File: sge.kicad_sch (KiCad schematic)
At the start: 27 parts, among them IC6 315-5660

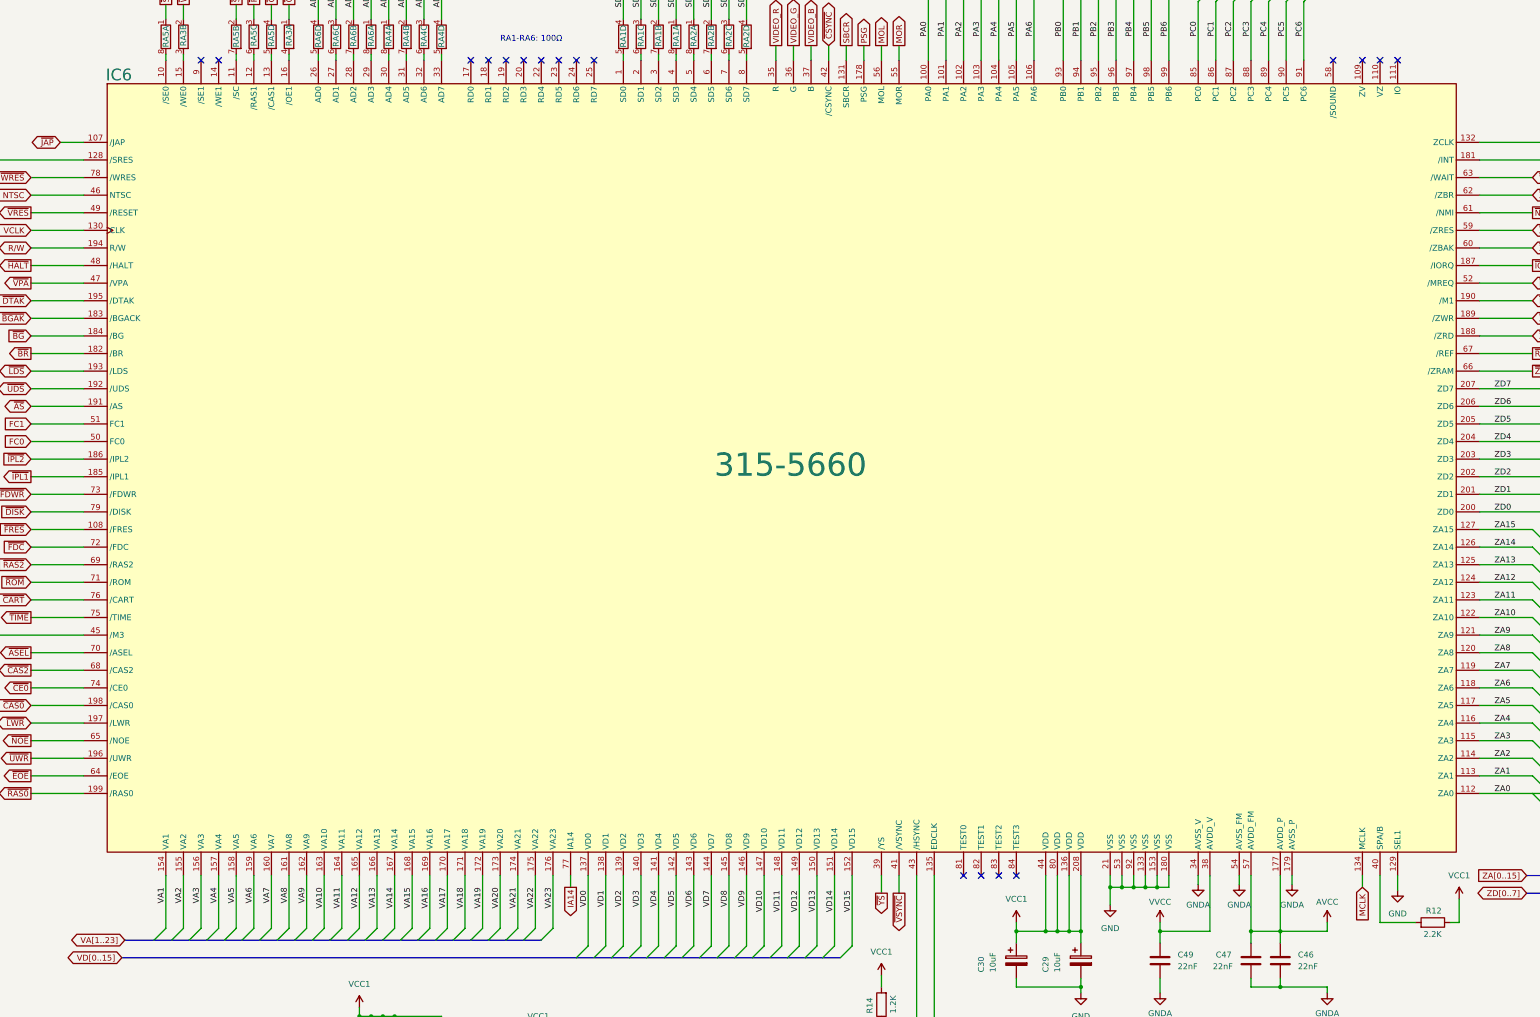
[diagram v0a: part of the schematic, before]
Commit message: update readme, update kicad version, add connection between 81 and GND
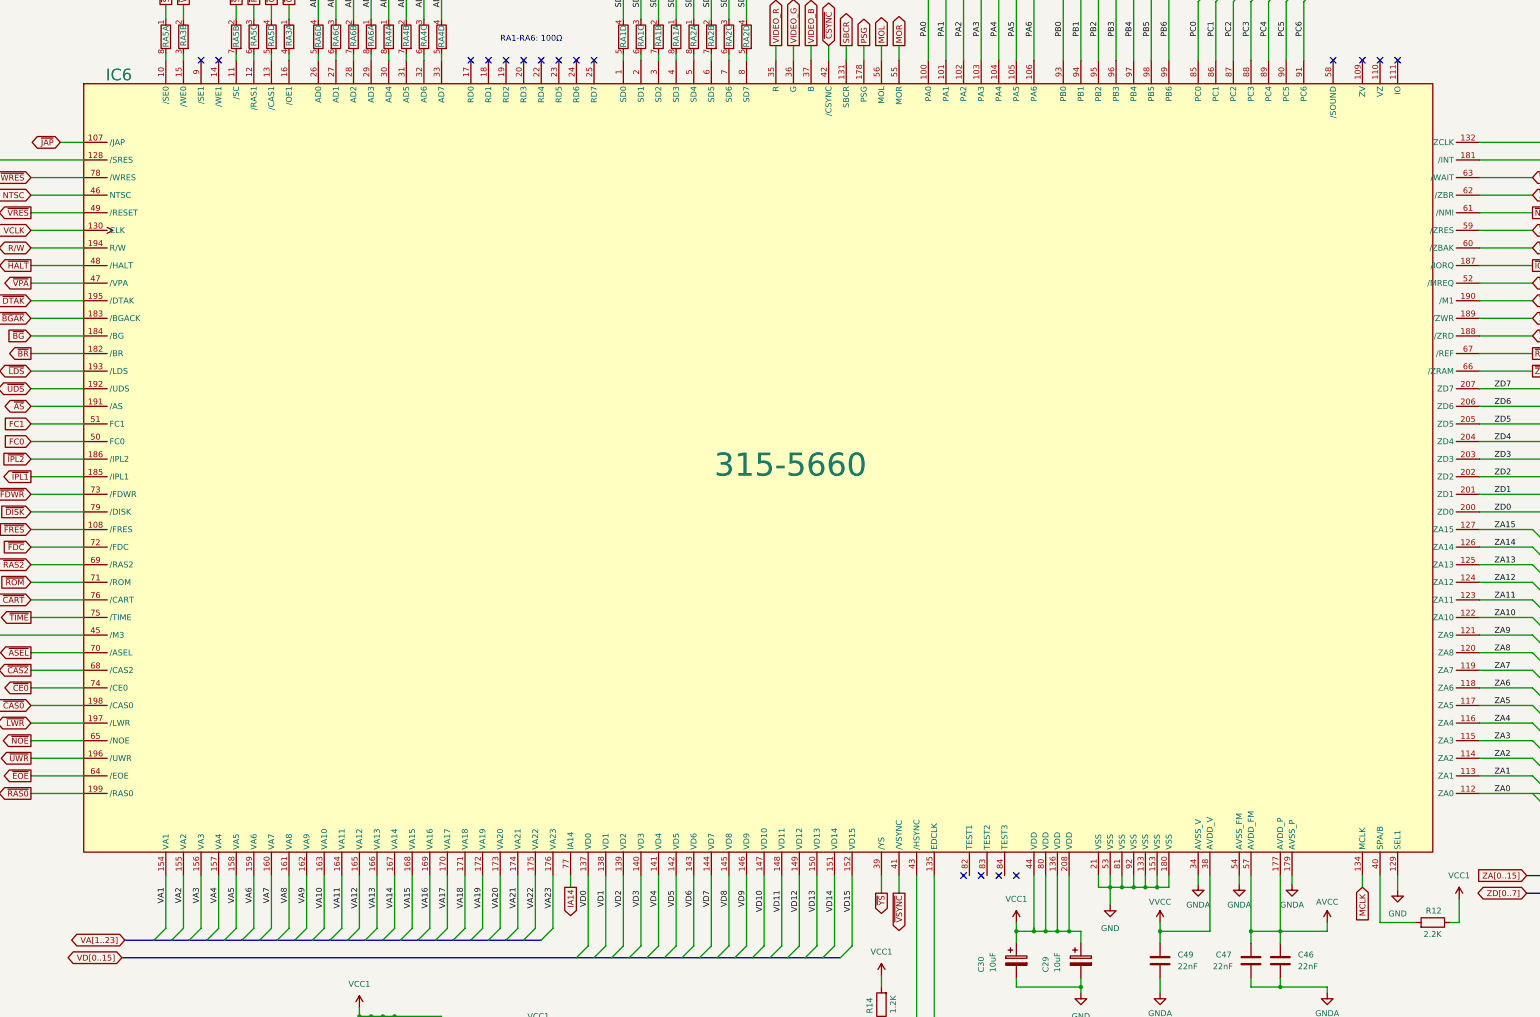
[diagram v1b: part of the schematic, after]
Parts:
- IC6: footprint Neptune:QFP-208_28x28_Pitch0.5mm -> Package_QFP:LQFP-208_28x28mm_P0.5mm
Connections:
- net GND: now also IC6.81 (VSS)
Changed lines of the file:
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@@
 (kicad_sch
-	(version 20231120)
+	(version 20250114)
 	(generator "eeschema")
-	(generator_version "8.0")
+	(generator_version "9.0")
 	(paper "A3")
 	(title_block
@@
 		(comment 1 "Neptune")
 	)
+	(text "Using 32X's RESET means we\ndon't need the whole /MRES\nto /SRES circuit from the MD."
+		(exclude_from_sim no)
+		(at 15.875 61.595 0)
+		(effects
+			(font
+				(size 1.27 1.27)
+			)
+			(justify left bottom)
+		)
+	)
+	(text "RA1-RA6: 100Ω"
+		(exclude_from_sim no)
+		(at 152.4 39.37 0)
+		(effects
+			(font
+				(size 1.27 1.27)
+			)
+			(justify left bottom)
+		)
+	)
 	(junction
 		(at 292.1 222.25)
@@
 	)
 	(junction
+		(at 267.965 231.775)
+		(diameter 0)
+		(color 0 0 0 0)
+	)
+	(junction
 		(at 127 250.19)
 		(diameter 0)
@@
 	)
 	(junction
-		(at 278.13 231.775)
-		(diameter 0)
-		(color 0 0 0 0)
-	)
-	(junction
 		(at 175.26 257.81)
 		(diameter 0)
@@
 	(wire
 		(pts
-			(xy 264.16 231.775) (xy 270.51 231.775)
+			(xy 264.16 231.775) (xy 267.965 231.775)
 		)
 		(stroke
@@
 	(wire
 		(pts
+			(xy 267.965 231.14) (xy 267.965 231.775)
+		)
+		(stroke
+			(width 0)
+			(type default)
+		)
+	)
+	(wire
+		(pts
 			(xy 303.53 219.71) (xy 303.53 221.615)
 		)
@@
 	(wire
 		(pts
-			(xy 87.63 219.71) (xy 87.63 231.14)
+			(xy 267.965 231.775) (xy 270.51 231.775)
 		)
 		(stroke
@@
 	(wire
 		(pts
-			(xy 50.8 133.35) (xy 62.23 133.35)
+			(xy 87.63 219.71) (xy 87.63 231.14)
 		)
 		(stroke
@@
 	(wire
 		(pts
-			(xy 201.93 219.71) (xy 201.93 234.95)
+			(xy 50.8 133.35) (xy 62.23 133.35)
 		)
 		(stroke
@@
 	(wire
 		(pts
-			(xy 50.8 99.06) (xy 62.23 99.06)
+			(xy 201.93 219.71) (xy 201.93 234.95)
 		)
 		(stroke
@@
 		)
 	)
-	(bus
+	(wire
 		(pts
-			(xy 378.46 158.75) (xy 378.46 162.56)
+			(xy 50.8 99.06) (xy 62.23 99.06)
 		)
 		(stroke
@@
 		)
 	)
-	(wire
+	(bus
 		(pts
-			(xy 190.5 41.91) (xy 190.5 43.18)
+			(xy 378.46 158.75) (xy 378.46 162.56)
 		)
 		(stroke
@@
 	(wire
 		(pts
-			(xy 278.13 219.71) (xy 278.13 231.775)
+			(xy 190.5 41.91) (xy 190.5 43.18)
 		)
 		(stroke
@@
 	(wire
 		(pts
+			(xy 267.97 231.14) (xy 267.965 231.14)
+		)
+		(stroke
+			(width 0)
+			(type default)
+		)
+	)
+	(wire
+		(pts
 			(xy 231.14 40.005) (xy 231.14 43.18)
 		)
@@
 	(wire
 		(pts
+			(xy 281.94 219.71) (xy 281.94 222.25)
+		)
+		(stroke
+			(width 0)
+			(type default)
+		)
+	)
+	(wire
+		(pts
 			(xy 234.95 40.005) (xy 234.95 43.18)
 		)
@@
 		)
 	)
+	(wire
+		(pts
+			(xy 281.94 222.25) (xy 284.48 222.25)
+		)
+		(stroke
+			(width 0)
+			(type default)
+		)
+	)
 	(bus
 		(pts
@@
 	(wire
 		(pts
-			(xy 198.12 41.91) (xy 198.12 43.18)
+			(xy 267.97 219.71) (xy 267.97 231.14)
 		)
 		(stroke
@@
 		)
 	)
-	(text "Using 32X's RESET means we\ndon't need the whole /MRES\nto /SRES circuit from the MD."
-		(exclude_from_sim no)
-		(at 15.875 61.595 0)
-		(effects
-			(font
-				(size 1.27 1.27)
-			)
-			(justify left bottom)
+	(wire
+		(pts
+			(xy 198.12 41.91) (xy 198.12 43.18)
 		)
-	)
-	(text "RA1-RA6: 100Ω"
-		(exclude_from_sim no)
-		(at 152.4 39.37 0)
-		(effects
-			(font
-				(size 1.27 1.27)
-			)
-			(justify left bottom)
+		(stroke
+			(width 0)
+			(type default)
 		)
 	)
@@
 			)
 		)
-		(property "Footprint" "Neptune:QFP-208_28x28_Pitch0.5mm"
+		(property "Footprint" "Package_QFP:LQFP-208_28x28mm_P0.5mm"
 			(at 212.09 135.89 0)
 			(effects
@@
 			)
 		)
-		(property "Description" ""
+		(property "Description" "SEGA MD2 VDP"
 			(at 213.36 130.81 0)
 			(effects
